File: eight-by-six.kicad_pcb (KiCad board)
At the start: 2 copper layers, 171.4 x 171.4 mm, 108 parts, among them J1 Left, J2 Right, SW1 Key, SW10 Key, SW11 Key, SW12 Key, SW13 Key, SW14 Key, SW15 Key, SW16 Key, SW17 Key, SW18 Key, SW19 Key, SW2 Key, SW20 Key, SW21 Key, SW22 Key, SW23 Key, SW24 Key, SW25 Key, SW26 Key, SW27 Key, SW28 Key, SW29 Key, SW3 Key, SW30 Key, SW31 Key, SW32 Key, SW33 Key, SW34 Key, SW35 Key, SW36 Key, SW37 Key, SW38 Key, SW39 Key, SW4 Key, SW40 Key, SW41 Key, SW42 Key, SW43 Key, SW44 Key, SW45 Key, SW46 Key, SW47 Key, SW48 Key, SW5 Key, SW6 Key, SW7 Key, SW8 Key, SW9 Key

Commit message: Done all measurement and cuts
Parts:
- removed D1, D10, D11, D12, D13, D14, D15, D16, D17, D18, D19, D2, D20, D21, D22, D23, D24, D25, D26, D27, D28, D29, D3, D30, D31, D32, D33, D34, D35, D36, D37, D38, D39, D4, D40, D41, D42, D43, D44, D45, D46, D47, D48, D5, D6, D7, D8, D9: 1N4148, commons-passives_THT:Passive_THT_diode_W2.54mm_L12.70mm
- removed the H1 at (23.8, 81.0)
- removed the H2 at (23.8, 109.5)
- removed H5, H6: M2.5, MountingHole:MountingHole_2.7mm_M2.5
- removed J1: Left, Connector_PinHeader_2.54mm:PinHeader_1x10_P2.54mm_Vertical
- removed J2: Right, Connector_PinHeader_2.54mm:PinHeader_1x12_P2.54mm_Vertical
- removed SW1, SW10, SW11, SW12, SW13, SW14, SW15, SW16, SW17, SW18, SW19, SW2, SW20, SW21, SW22, SW23, SW24, SW25, SW26, SW27, SW28, SW29, SW3, SW30, SW31, SW32, SW33, SW34, SW35, SW36, SW37, SW38, SW39, SW4, SW40, SW41, SW42, SW43, SW44, SW45, SW46, SW47, SW48, SW5, SW6, SW7, SW8, SW9: Key, key-switches:SW_MX_THT
- renumbered H3 to H1, H4 to H2, H7 to H3, H8 to H4
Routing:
- net /r5: track 282.8 -> 0.00 mm
- net /r4: track 260.8 -> 0.00 mm
- net /r2: track 246.9 -> 0.00 mm, vias 1 -> 0
- net /r3: track 239.2 -> 0.00 mm
- net /r1: track 225.2 -> 0.00 mm, vias 1 -> 0
- net /c3: track 204.6 -> 0.00 mm, vias 2 -> 0
- net /r0: track 203.1 -> 0.00 mm, vias 1 -> 0
- net /c4: track 192.1 -> 0.00 mm, vias 2 -> 0
- net /c2: track 184.1 -> 0.00 mm, vias 2 -> 0
- net /c5: track 171.5 -> 0.00 mm, vias 2 -> 0
- net /c1: track 163.5 -> 0.00 mm, vias 2 -> 0
- net /c6: track 150.5 -> 0.00 mm, vias 2 -> 0
- net /c0: track 142.9 -> 0.00 mm
- net /c7: track 138.0 -> 0.00 mm
- net Net-(D9-K): track 5.85 -> 0.00 mm
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- added copper zone on B.Cu, net (none)
- added copper zone on F.Cu, net (none)
- removed copper zone on B.Cu, net GND
- removed copper zone on F.Cu, net GND
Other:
- board size 171.4 x 171.4 mm -> 171.4 x 133.4 mm

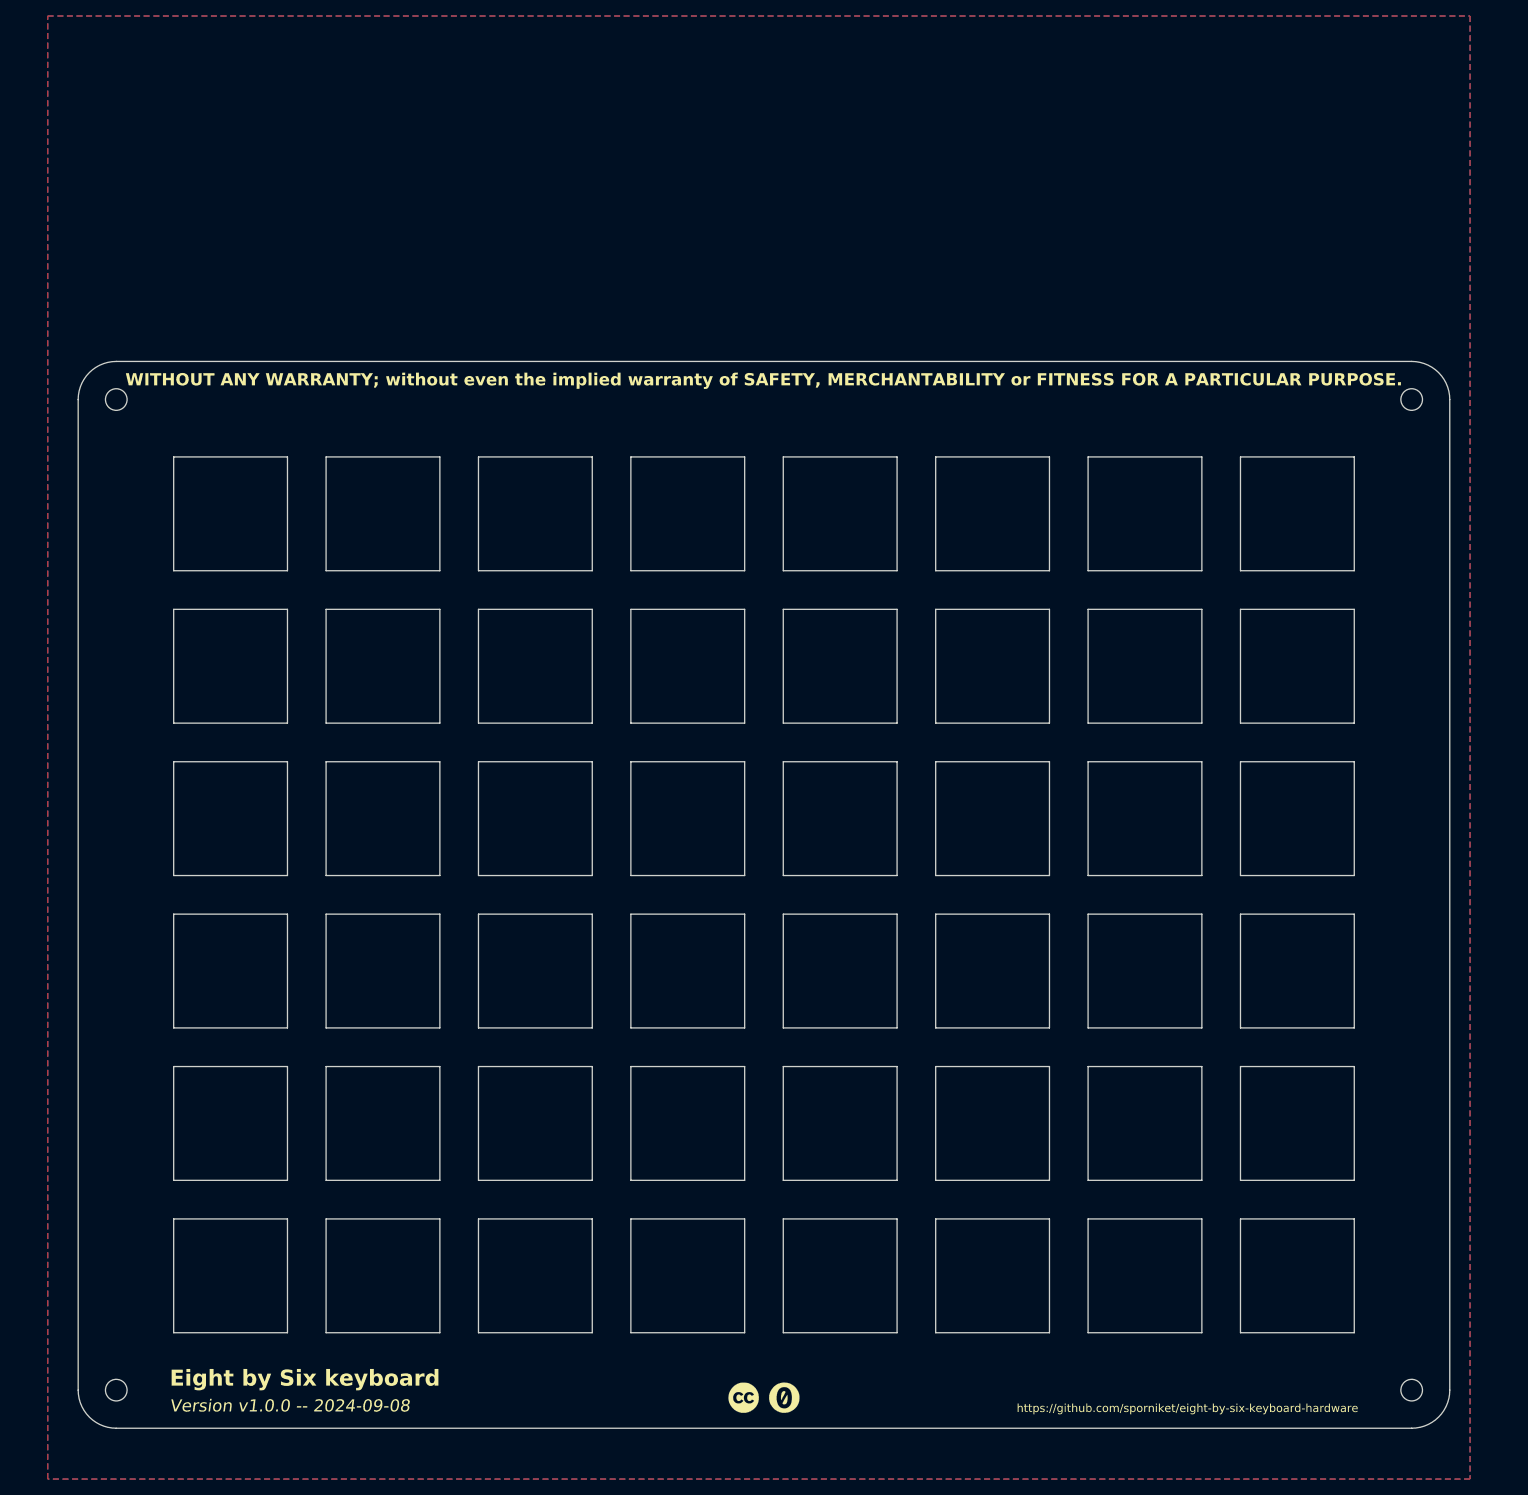
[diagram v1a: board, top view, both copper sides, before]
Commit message: change the mention of 'hardware' to 'plate', adjust the look of the plate
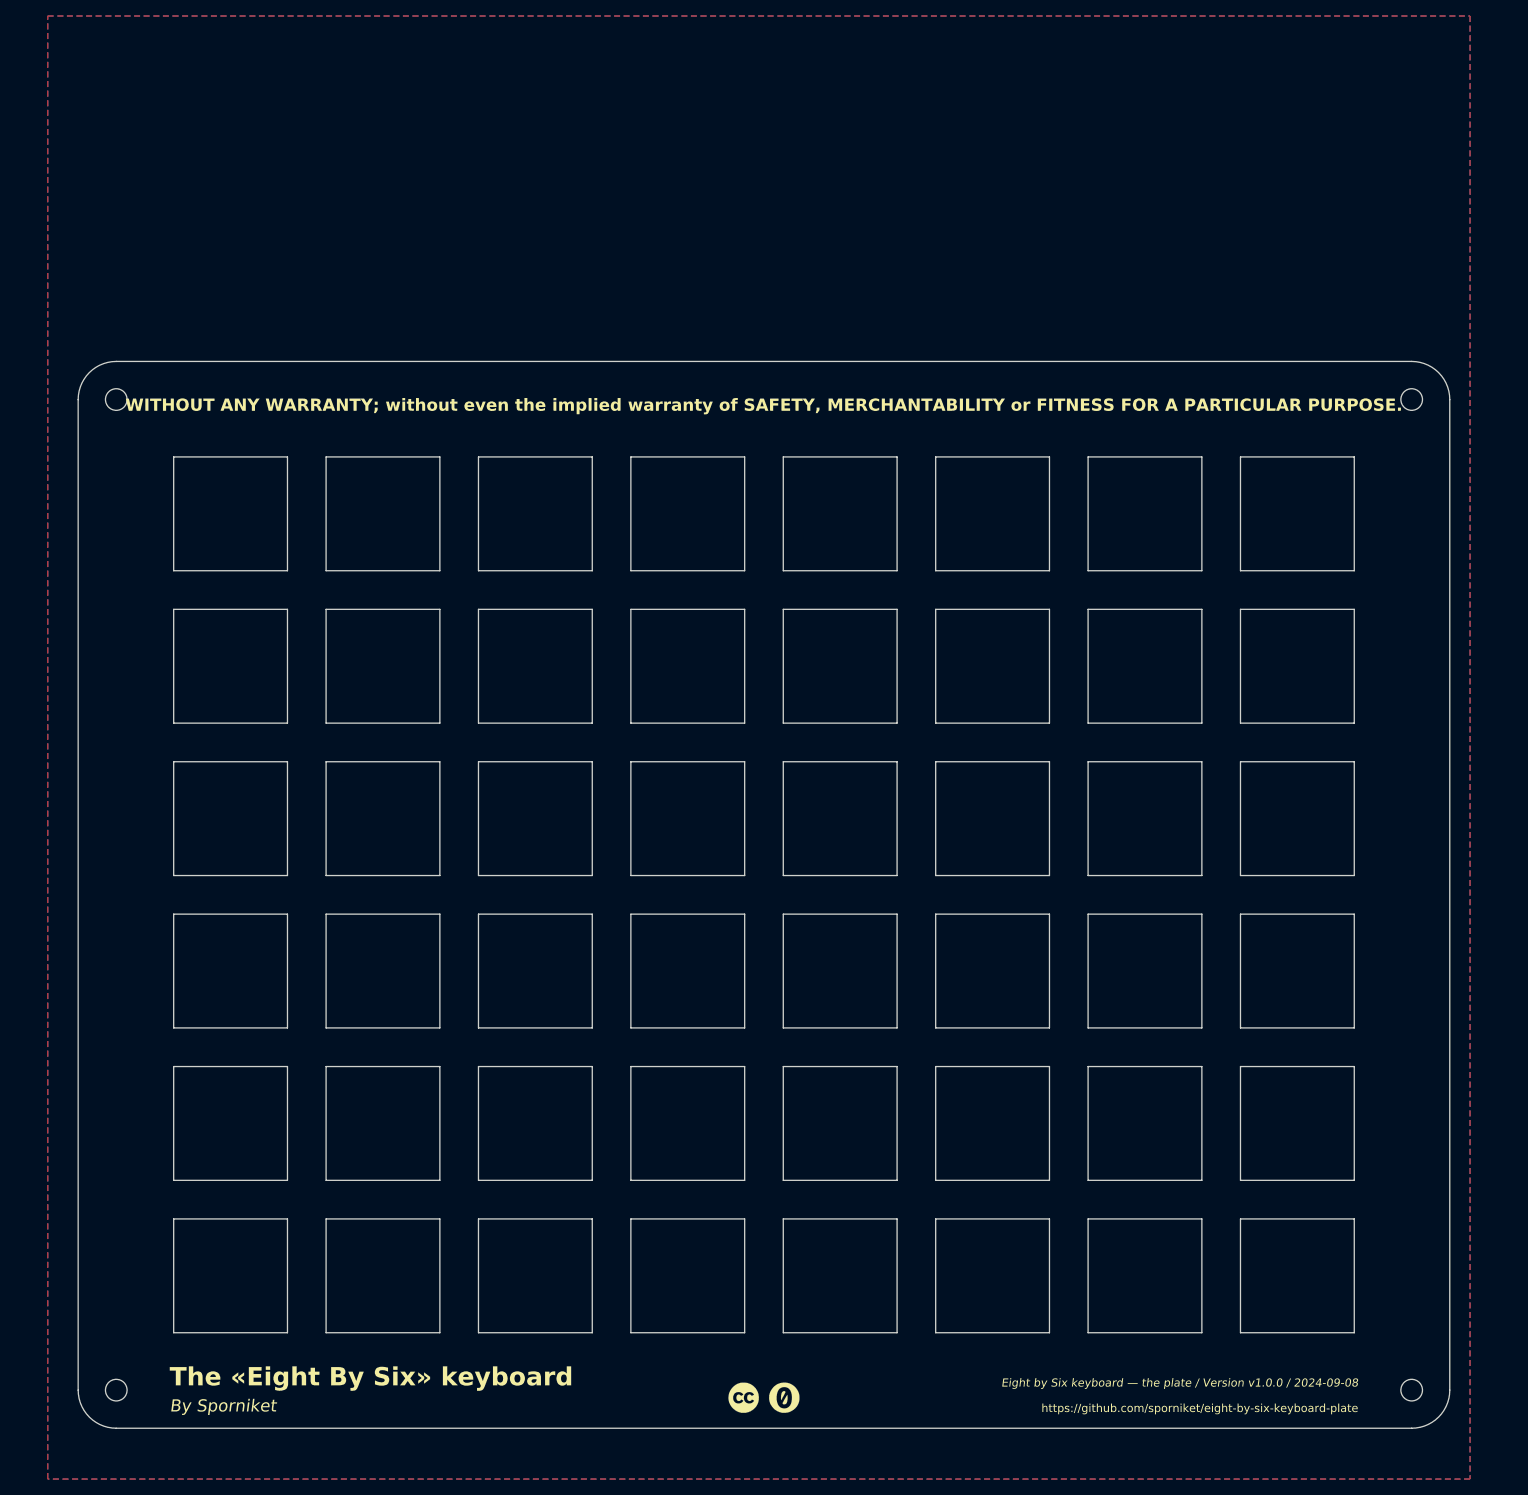
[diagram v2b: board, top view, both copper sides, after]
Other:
- board text added: "${TITLE} / Version ${REVISION} / ${ISSUE_DATE}"
- board text added: "By ${COMPANY}"
- board text added: "The «Eight By Six» keyboard"
- board text removed: "${TITLE}"
- board text removed: "Version ${REVISION} -- ${ISSUE_DATE}"
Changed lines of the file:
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@@
   (paper "A4" portrait)
   (title_block
-    (title "Eight by Six keyboard")
+    (title "Eight by Six keyboard — the plate")
     (date "2024-09-08")
     (rev "v1.0.0")
     (company "Sporniket")
     (comment 1 "All dimensions are in mm. Tolerance depends on manufacturer.")
-    (comment 3 "https://github.com/sporniket/eight-by-six-keyboard-hardware")
+    (comment 3 "https://github.com/sporniket/eight-by-six-keyboard-plate")
     (comment 4 "Original repository :")
   )
@@
     (effects (font (size 1.016 1.016) (thickness 0.1524)) (justify right bottom))
   )
-  (gr_text "WITHOUT ANY WARRANTY; without even the implied warranty of SAFETY, MERCHANTABILITY or FITNESS FOR A PARTICULAR PURPOSE." (at 104.775 117.475) (layer "F.SilkS")
+  (gr_text "WITHOUT ANY WARRANTY; without even the implied warranty of SAFETY, MERCHANTABILITY or FITNESS FOR A PARTICULAR PURPOSE." (at 104.775 120.65) (layer "F.SilkS")
     (effects (font (size 1.524 1.524) (thickness 0.3048) bold) (justify bottom))
   )
-  (gr_text "Version ${REVISION} -- ${ISSUE_DATE}" (at 30.48 245.745) (layer "F.SilkS")
+  (gr_text "By ${COMPANY}" (at 30.48 245.745) (layer "F.SilkS")
     (effects (font (size 1.524 1.524) (thickness 0.2286) italic) (justify left bottom))
   )
-  (gr_text "${TITLE}" (at 30.48 242.57) (layer "F.SilkS")
-    (effects (font (size 2 2) (thickness 0.4) bold) (justify left bottom))
+  (gr_text "${TITLE} / Version ${REVISION} / ${ISSUE_DATE}" (at 179.07 242.57) (layer "F.SilkS")
+    (effects (font (size 1.016 1.016) (thickness 0.1524) italic) (justify right bottom))
+  )
+  (gr_text "The «Eight By Six» keyboard" (at 30.48 242.57) (layer "F.SilkS")
+    (effects (font (size 2.286 2.286) (thickness 0.4572) bold) (justify left bottom))
   )
   (dimension (type aligned) (layer "User.1")
     (pts (xy 19.05 145.288) (xy 19.05 140.462))
     (height -1.27)
-    (gr_text "4,8" (at 16.63 142.875 90) (layer "User.1")
+    (gr_text "4.8" (at 16.63 142.875 90) (layer "User.1")
       (effects (font (size 1 1) (thickness 0.15)))
     )
@@
     (pts (xy 19.05 140.462) (xy 19.05 126.238))
     (height -1.27)
-    (gr_text "14,2 mm" (at 16.63 133.35 90) (layer "User.1")
+    (gr_text "14.2 mm" (at 16.63 133.35 90) (layer "User.1")
       (effects (font (size 1 1) (thickness 0.15)))
     )
@@
     (pts (xy 19.05 235.712) (xy 19.05 221.488))
     (height -1.27)
-    (gr_text "14,2 mm" (at 16.63 228.6 90) (layer "User.1")
+    (gr_text "14.2 mm" (at 16.63 228.6 90) (layer "User.1")
       (effects (font (size 1 1) (thickness 0.15)))
     )
@@
     (pts (xy 19.05 221.488) (xy 19.05 216.662))
     (height -1.27)
-    (gr_text "4,8" (at 16.63 219.075 90) (layer "User.1")
+    (gr_text "4.8" (at 16.63 219.075 90) (layer "User.1")
       (effects (font (size 1 1) (thickness 0.15)))
     )
@@
     (pts (xy 30.988 247.65) (xy 45.212 247.65))
     (height 3.048)
-    (gr_text "14,2 mm" (at 38.1 249.548) (layer "User.1")
+    (gr_text "14.2 mm" (at 38.1 249.548) (layer "User.1")
       (effects (font (size 1 1) (thickness 0.15)))
     )
@@
     (pts (xy 126.238 247.65) (xy 121.412 247.65))
     (height -3.048)
-    (gr_text "4,8" (at 123.825 249.548) (layer "User.1")
+    (gr_text "4.8" (at 123.825 249.548) (layer "User.1")
       (effects (font (size 1 1) (thickness 0.15)))
     )
@@
     (pts (xy 19.05 247.65) (xy 30.988 247.65))
     (height 3.048)
-    (gr_text "11,9 mm" (at 25.019 249.548) (layer "User.1")
+    (gr_text "11.9 mm" (at 25.019 249.548) (layer "User.1")
       (effects (font (size 1 1) (thickness 0.15)))
     )
@@
     (pts (xy 19.05 114.3) (xy 190.5 114.3))
     (height -4.445)
-    (gr_text "171,4 mm" (at 104.775 108.705) (layer "User.1")
+    (gr_text "171.4 mm" (at 104.775 108.705) (layer "User.1")
       (effects (font (size 1 1) (thickness 0.15)))
     )
@@
     (pts (xy 145.288 247.65) (xy 159.512 247.65))
     (height 3.048)
-    (gr_text "14,2 mm" (at 152.4 249.548) (layer "User.1")
+    (gr_text "14.2 mm" (at 152.4 249.548) (layer "User.1")
       (effects (font (size 1 1) (thickness 0.15)))
     )
@@
     (pts (xy 107.188 247.65) (xy 102.362 247.65))
     (height -3.048)
-    (gr_text "4,8" (at 104.775 249.548) (layer "User.1")
+    (gr_text "4.8" (at 104.775 249.548) (layer "User.1")
       (effects (font (size 1 1) (thickness 0.15)))
     )
@@
     (pts (xy 185.7375 114.3) (xy 190.5 114.3))
     (height -1.905)
-    (gr_text "4,8" (at 188.11875 111.245) (layer "User.1")
+    (gr_text "4.8" (at 188.11875 111.245) (layer "User.1")
       (effects (font (size 1 1) (thickness 0.15)))
     )
@@
     (pts (xy 19.05 247.65) (xy 19.05 235.712))
     (height -1.27)
-    (gr_text "11,9 mm" (at 16.63 241.681 90) (layer "User.1")
+    (gr_text "11.9 mm" (at 16.63 241.681 90) (layer "User.1")
       (effects (font (size 1 1) (thickness 0.15)))
     )
@@
     (pts (xy 19.05 164.338) (xy 19.05 159.512))
     (height -1.27)
-    (gr_text "4,8" (at 16.63 161.925 90) (layer "User.1")
+    (gr_text "4.8" (at 16.63 161.925 90) (layer "User.1")
       (effects (font (size 1 1) (thickness 0.15)))
     )
@@
     (pts (xy 19.05 183.388) (xy 19.05 178.562))
     (height -1.27)
-    (gr_text "4,8" (at 16.63 180.975 90) (layer "User.1")
+    (gr_text "4.8" (at 16.63 180.975 90) (layer "User.1")
       (effects (font (size 1 1) (thickness 0.15)))
     )
@@
     (pts (xy 19.05 197.612) (xy 19.05 183.388))
     (height -1.27)
-    (gr_text "14,2 mm" (at 16.63 190.5 90) (layer "User.1")
+    (gr_text "14.2 mm" (at 16.63 190.5 90) (layer "User.1")
       (effects (font (size 1 1) (thickness 0.15)))
     )
@@
     (pts (xy 126.238 247.65) (xy 140.462 247.65))
     (height 3.048)
-    (gr_text "14,2 mm" (at 133.35 249.548) (layer "User.1")
+    (gr_text "14.2 mm" (at 133.35 249.548) (layer "User.1")
       (effects (font (size 1 1) (thickness 0.15)))
     )
@@
     (pts (xy 69.088 247.65) (xy 64.262 247.65))
     (height -3.048)
-    (gr_text "4,8" (at 66.675 249.548) (layer "User.1")
+    (gr_text "4.8" (at 66.675 249.548) (layer "User.1")
       (effects (font (size 1 1) (thickness 0.15)))
     )
@@
     (pts (xy 164.338 247.65) (xy 178.562 247.65))
     (height 3.048)
-    (gr_text "14,2 mm" (at 171.45 249.548) (layer "User.1")
+    (gr_text "14.2 mm" (at 171.45 249.548) (layer "User.1")
       (effects (font (size 1 1) (thickness 0.15)))
     )
@@
     (pts (xy 19.05 178.562) (xy 19.05 164.338))
     (height -1.27)
-    (gr_text "14,2 mm" (at 16.63 171.45 90) (layer "User.1")
+    (gr_text "14.2 mm" (at 16.63 171.45 90) (layer "User.1")
       (effects (font (size 1 1) (thickness 0.15)))
     )
@@
     (pts (xy 164.338 247.65) (xy 159.512 247.65))
     (height -3.048)
-    (gr_text "4,8" (at 161.925 249.548) (layer "User.1")
+    (gr_text "4.8" (at 161.925 249.548) (layer "User.1")
       (effects (font (size 1 1) (thickness 0.15)))
     )
@@
     (pts (xy 88.138 247.65) (xy 83.312 247.65))
     (height -3.048)
-    (gr_text "4,8" (at 85.725 249.548) (layer "User.1")
+    (gr_text "4.8" (at 85.725 249.548) (layer "User.1")
       (effects (font (size 1 1) (thickness 0.15)))
     )
@@
     (pts (xy 19.05 114.3) (xy 23.8125 114.3))
     (height -1.905)
-    (gr_text "4,8" (at 21.43125 111.245) (layer "User.1")
+    (gr_text "4.8" (at 21.43125 111.245) (layer "User.1")
       (effects (font (size 1 1) (thickness 0.15)))
     )
@@
     (pts (xy 50.038 247.65) (xy 45.212 247.65))
     (height -3.048)
-    (gr_text "4,8" (at 47.625 249.548) (layer "User.1")
+    (gr_text "4.8" (at 47.625 249.548) (layer "User.1")
       (effects (font (size 1 1) (thickness 0.15)))
     )
@@
     (pts (xy 88.138 247.65) (xy 102.362 247.65))
     (height 3.048)
-    (gr_text "14,2 mm" (at 95.25 249.548) (layer "User.1")
+    (gr_text "14.2 mm" (at 95.25 249.548) (layer "User.1")
       (effects (font (size 1 1) (thickness 0.15)))
     )
@@
     (pts (xy 19.05 159.512) (xy 19.05 145.288))
     (height -1.27)
-    (gr_text "14,2 mm" (at 16.63 152.4 90) (layer "User.1")
+    (gr_text "14.2 mm" (at 16.63 152.4 90) (layer "User.1")
       (effects (font (size 1 1) (thickness 0.15)))
     )
@@
     (pts (xy 50.038 247.65) (xy 64.262 247.65))
     (height 3.048)
-    (gr_text "14,2 mm" (at 57.15 249.548) (layer "User.1")
+    (gr_text "14.2 mm" (at 57.15 249.548) (layer "User.1")
       (effects (font (size 1 1) (thickness 0.15)))
     )
@@
     (pts (xy 107.188 247.65) (xy 121.412 247.65))
     (height 3.048)
-    (gr_text "14,2 mm" (at 114.3 249.548) (layer "User.1")
+    (gr_text "14.2 mm" (at 114.3 249.548) (layer "User.1")
       (effects (font (size 1 1) (thickness 0.15)))
     )
@@
     (pts (xy 19.05 202.438) (xy 19.05 197.612))
     (height -1.27)
-    (gr_text "4,8" (at 16.63 200.025 90) (layer "User.1")
+    (gr_text "4.8" (at 16.63 200.025 90) (layer "User.1")
       (effects (font (size 1 1) (thickness 0.15)))
     )
@@
     (pts (xy 145.288 247.65) (xy 140.462 247.65))
     (height -3.048)
-    (gr_text "4,8" (at 142.875 249.548) (layer "User.1")
+    (gr_text "4.8" (at 142.875 249.548) (layer "User.1")
       (effects (font (size 1 1) (thickness 0.15)))
     )
@@
     (pts (xy 69.088 247.65) (xy 83.312 247.65))
     (height 3.048)
-    (gr_text "14,2 mm" (at 76.2 249.548) (layer "User.1")
+    (gr_text "14.2 mm" (at 76.2 249.548) (layer "User.1")
       (effects (font (size 1 1) (thickness 0.15)))
     )
@@
     (pts (xy 19.05 216.662) (xy 19.05 202.438))
     (height -1.27)
-    (gr_text "14,2 mm" (at 16.63 209.55 90) (layer "User.1")
-      (effects (font (size 1 1) (thickness 0.15)))
-    )
+    (gr_text "14.2 mm" (at 16.63 209.55 90) (layer "User.1")
+      (effects (font (size 1 1) (thickness 0.15)))
+    )
